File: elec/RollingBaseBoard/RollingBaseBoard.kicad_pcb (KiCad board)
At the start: 2 copper layers, 98 parts, among them P1 GP2, P10 UART_2, P11 I2C, P12 Motor, P13 Motor, P14 Encoder2, P15 Motor, P16 Switch, P17 Switch, P18 Switch, P19 Switch, P2 GP2, P20 Switch, P3 GP2, P4 GP2, P5 Bat5V, P6 Bat15V, P7 Encoder, P8 Encoder, P9 UART_1, U1 LMD18201, U2 LMD18201, U3 Teensy3.1

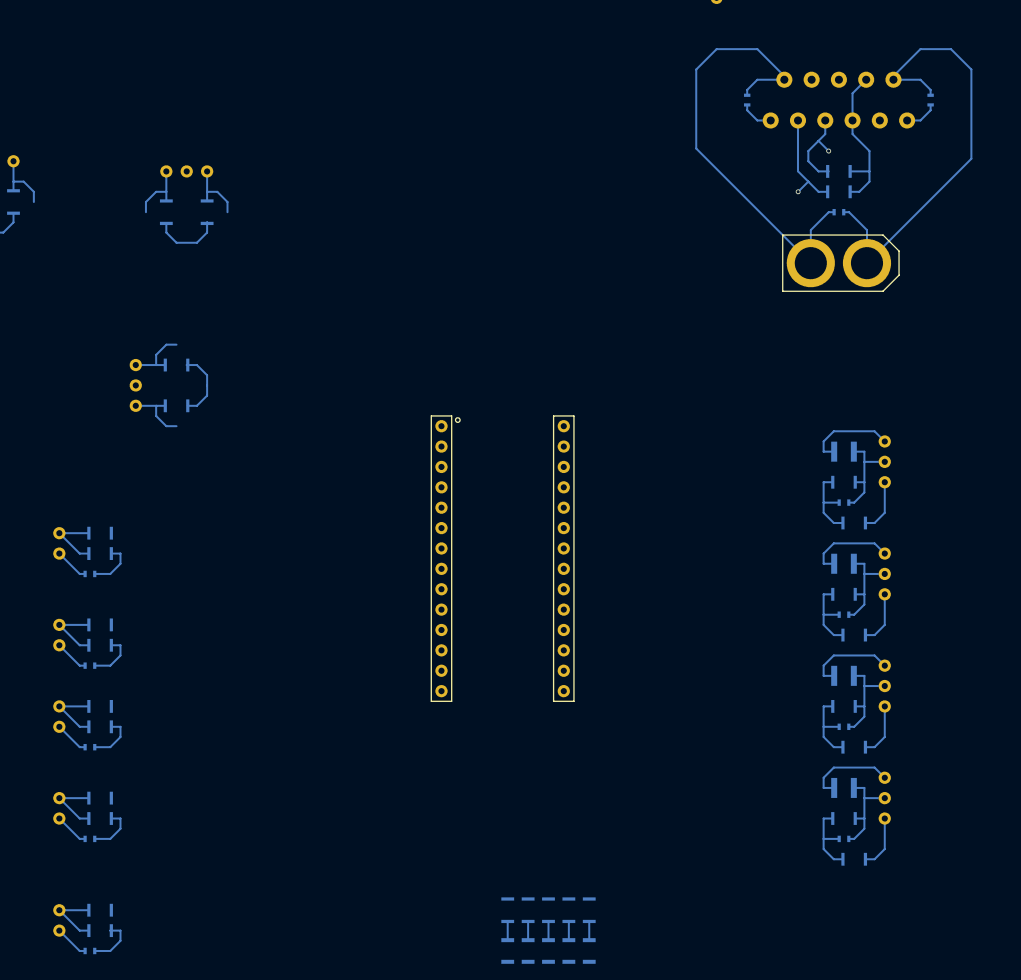
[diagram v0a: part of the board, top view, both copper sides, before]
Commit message: Progressing on rolling base board's routing
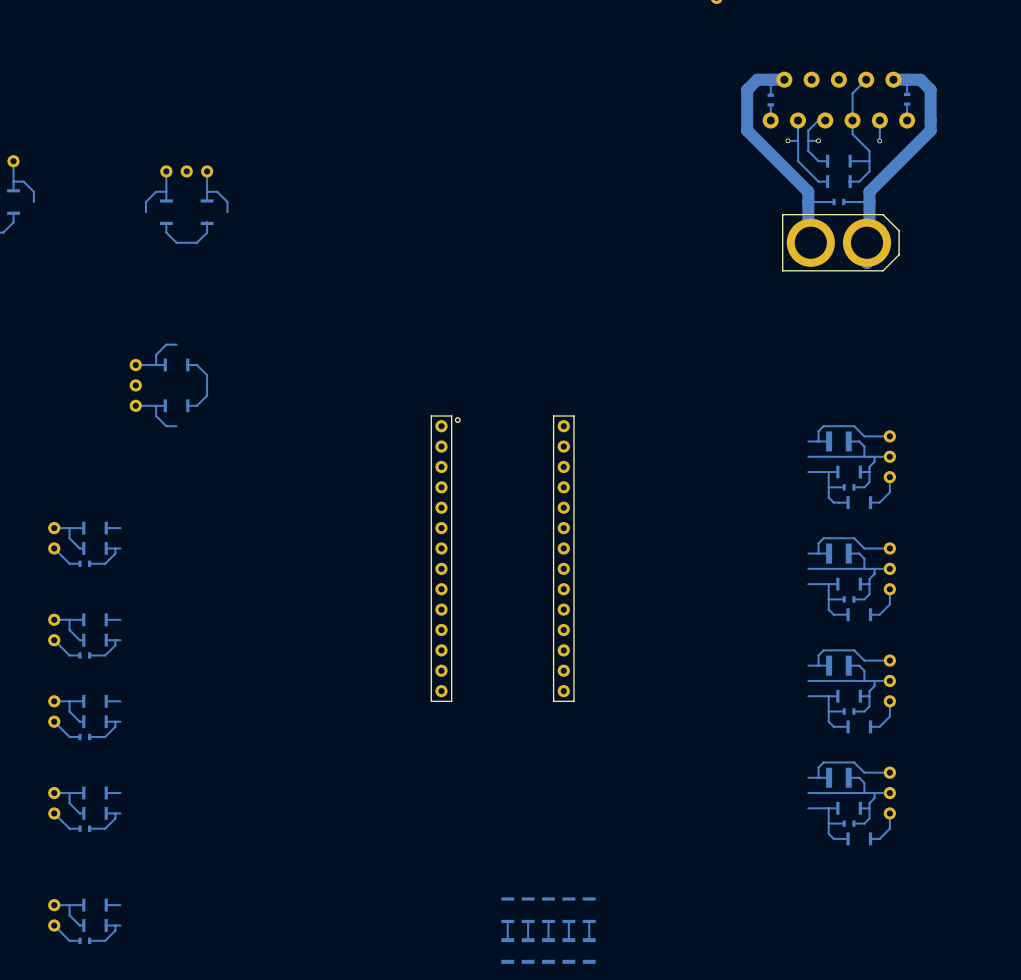
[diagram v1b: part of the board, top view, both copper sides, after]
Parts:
- moved C19 2.94 mm to (159.2, 38.1)
- moved C20 2.92 mm to (176.2, 38.0)
- moved R4 2.62 mm to (170.2, 116.2)
- moved R6 2.62 mm to (170.2, 102.2)
- moved R8 2.62 mm to (170.2, 88.3)
- moved R2 2.62 mm to (170.2, 130.2)
- moved P13 2.54 mm to (167.6, 55.9)
- moved C2 2.01 mm to (168.9, 128.3)
- moved C4 2.01 mm to (168.9, 114.3)
- moved C6 2.01 mm to (168.9, 100.3)
- moved C8 2.01 mm to (168.9, 86.4)
- moved C3 1.42 mm to (167.6, 108.6)
- moved C5 1.42 mm to (167.6, 94.6)
- moved C7 1.42 mm to (167.6, 80.6)
- moved C21 1.42 mm to (73.7, 142.9)
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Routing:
- net /Com/GND: track 142.9 -> 172.1 mm
- net Net-(C18-Pad2): track 57.7 -> 33.5 mm
- net Net-(C18-Pad1): track 55.9 -> 33.4 mm
- net /Com/+5V: track 84.8 -> 102.8 mm
- net /Driver_1/ThermalFlag: track 2.41 -> 4.96 mm, vias 0 -> 1
- net /Driver_2/PWM: track 11.7 -> 9.38 mm
- net Net-(C19-Pad1): track 4.13 -> 1.94 mm
- net Net-(C20-Pad2): track 4.13 -> 2.04 mm
- net Net-(P4-Pad1): track 6.75 -> 4.84 mm
- net Net-(P3-Pad1): track 6.75 -> 4.84 mm
- net Net-(P2-Pad1): track 6.75 -> 4.84 mm
- net Net-(P1-Pad1): track 6.75 -> 4.84 mm
- net /Driver_2/Direction: track 12.9 -> 11.1 mm
- net /Teensy/GP2_1: track 9.83 -> 11.5 mm
- net /Teensy/GP2_2: track 9.83 -> 11.5 mm
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
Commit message: Progressing on rolling base board's routing
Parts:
- added REF**: M4_Screw, Footprints:M4_Screw, F.Cu at (111.5, 142.0)
- added REF**: M4_Screw, Footprints:M4_Screw, F.Cu at (111.5, 68.0)
- added REF**: M4_Screw, Footprints:M4_Screw, F.Cu at (185.5, 68.0)
- added REF**: M4_Screw, Footprints:M4_Screw, F.Cu at (185.5, 142.0)
- D1, D2, D3, D4, D5, R28, R29, R30, R31, R32: moved to F.Cu
- moved P8 172.8 mm to (186.6, 78.3), turned to 270 degrees
- moved C10 166.7 mm to (182.8, 75.8), turned to 90 degrees
- moved R16 158.7 mm to (179.0, 79.6), turned to 180 degrees
- moved R17 158.7 mm to (179.0, 82.1), turned to 180 degrees
- moved R14 148.6 mm to (173.9, 79.6), turned to 0 degrees
- moved R15 148.5 mm to (173.9, 82.1), turned to 0 degrees
- moved P14 139.6 mm to (170.1, 80.9), turned to 90 degrees
- moved P16 117.3 mm to (146.0, 50.4), turned to 0 degrees
- moved C21 114.6 mm to (144.7, 52.9), turned to 90 degrees
- moved R34 113.9 mm to (147.2, 52.9), turned to 90 degrees
- moved R33 113.6 mm to (149.8, 52.9), turned to 90 degrees
- moved P5 104.8 mm to (148.5, 66.9)
- moved P18 102.9 mm to (161.2, 66.9), turned to 0 degrees
- moved C9 101.4 mm to (114.2, 80.9)
- moved R10 100.5 mm to (125.6, 77.1)
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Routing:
- net /Com/GND: track 172.1 -> 273.9 mm, vias 0 -> 13
- net /Com/+5V: track 102.8 -> 195.4 mm, vias 0 -> 7
- net Net-(P16-Pad2): track 7.25 -> 0.00 mm
- net /Teensy/Pull: track 6.28 -> 0.00 mm
- net /Teensy/LimitSwitch1: track 6.15 -> 9.96 mm
- net /Teensy/GP2_2: track 11.5 -> 14.7 mm
- net Net-(P3-Pad1): track 4.84 -> 2.41 mm
- net Net-(P2-Pad1): track 4.84 -> 2.41 mm
- net Net-(P4-Pad1): track 4.84 -> 6.75 mm
- net /Teensy/GP2_4: track 11.5 -> 9.98 mm
- net /Encoder_2/B: track 3.68 -> 2.41 mm
- net /Encoder_2/A: track 3.68 -> 2.41 mm
- net Net-(P8-Pad3): track 15.1 -> 16.3 mm
- net /Teensy/LimitSwitch2: track 6.15 -> 7.42 mm
- net Net-(P1-Pad1): track 4.84 -> 3.68 mm
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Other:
- board outline added: 80 x 80 mm

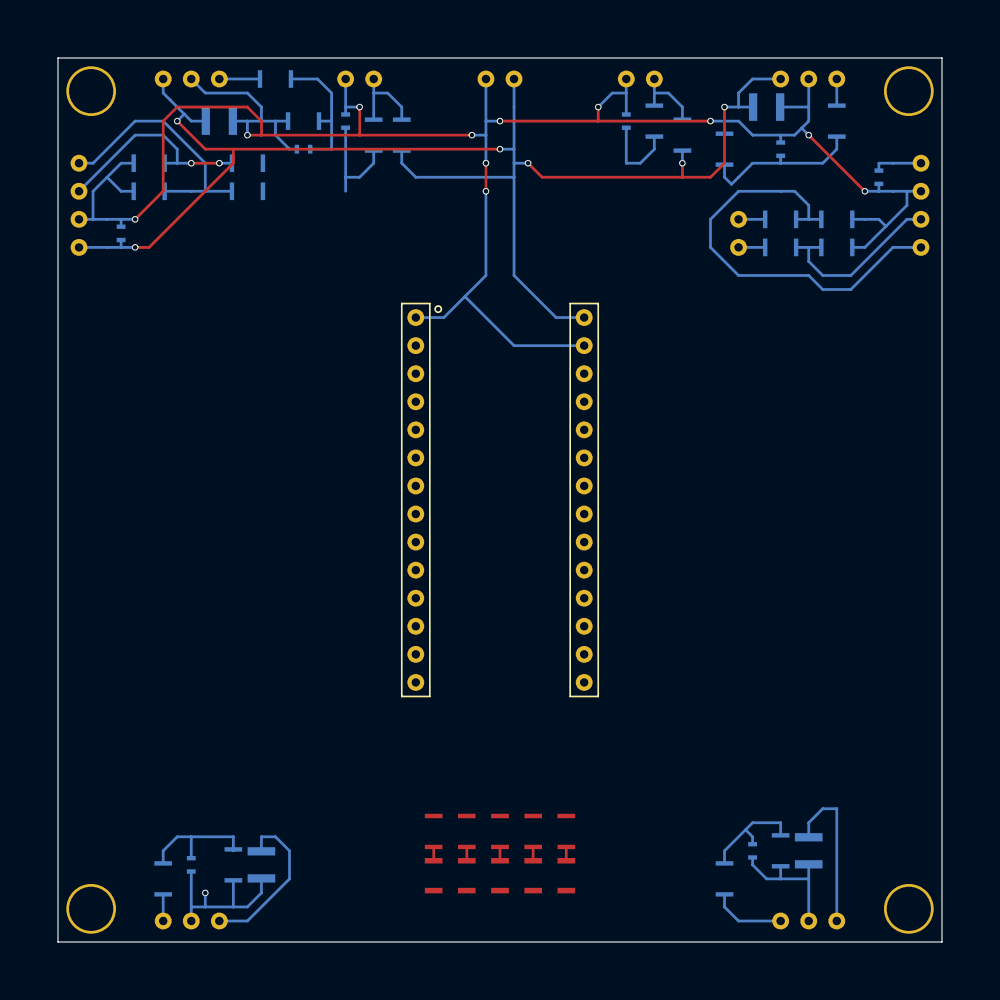
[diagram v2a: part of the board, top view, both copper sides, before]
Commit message: Replacing M4 screws with M3 ones
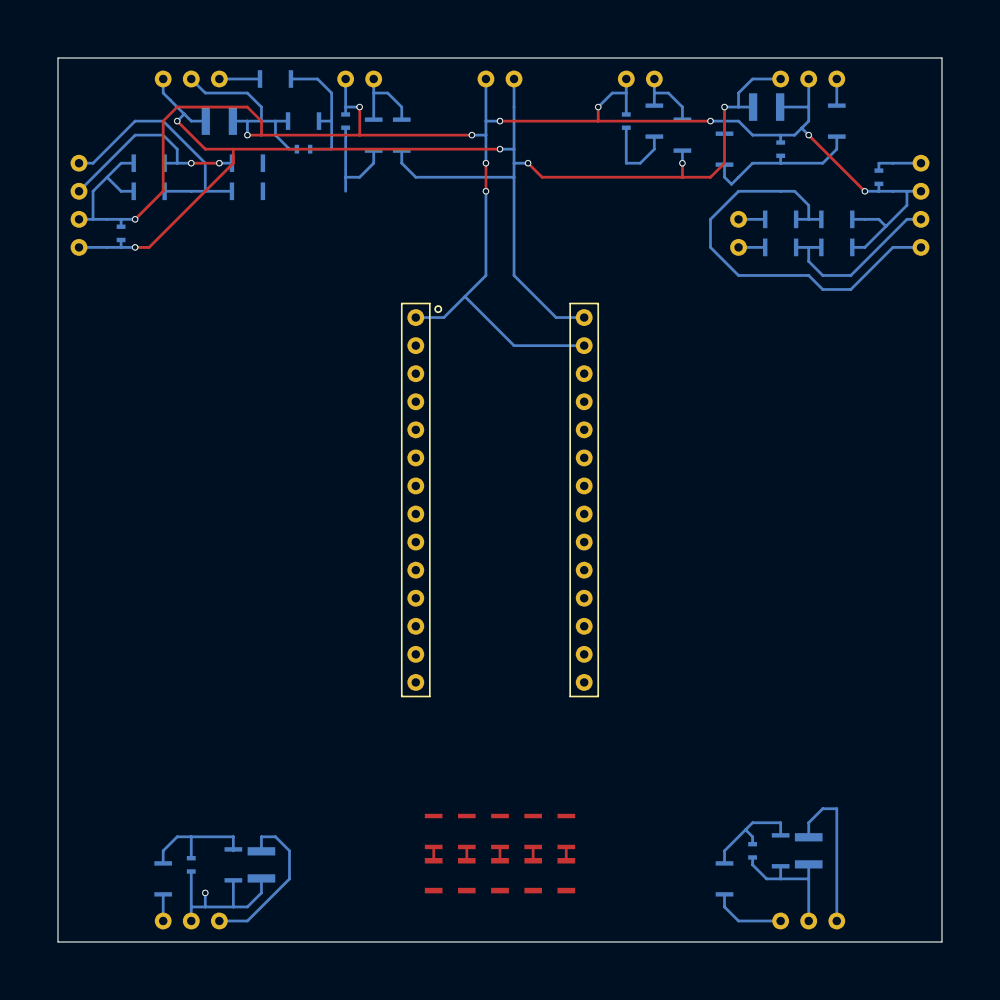
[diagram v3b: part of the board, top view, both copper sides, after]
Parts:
- removed REF** (x4): M4_Screw, Footprints:M4_Screw
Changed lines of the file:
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@@
-(kicad_pcb (version 4) (host pcbnew "(2015-09-24 BZR 6216, Git 45a9b1c)-product")
+(kicad_pcb (version 4) (host pcbnew 0.201509251831+6217~30~ubuntu15.04.1-product)
   (general
     (links 192)
     (no_connects 77)
-    (area 11.075 11.075 249.245002 148.277143)
+    (area 34.495 26.198 287.555002 163.625)
     (thickness 1.6)
     (drawings 4)
     (tracks 459)
     (zones 0)
-    (modules 102)
+    (modules 98)
     (nets 61)
   )
@@
       (net 57 "Net-(R30-Pad1)"))
   )
-  (module Footprints:M4_Screw (layer F.Cu)
-    (at 111.5 142)
-    (fp_text reference REF** (at 0 3.04) (layer F.SilkS) hide
-      (effects (font (size 1 1) (thickness 0.15)))
-    )
-    (fp_text value M4_Screw (at 0 -3.04) (layer F.Fab) hide
-      (effects (font (size 1 1) (thickness 0.15)))
-    )
-    (pad 1 thru_hole circle (at 0 0) (size 4.5 4.5) (drill 4) (layers *.Cu *.Mask F.SilkS))
-  )
-  (module Footprints:M4_Screw (layer F.Cu)
-    (at 111.5 68)
-    (fp_text reference REF** (at 0 3.04) (layer F.SilkS) hide
-      (effects (font (size 1 1) (thickness 0.15)))
-    )
-    (fp_text value M4_Screw (at 0 -3.04) (layer F.Fab) hide
-      (effects (font (size 1 1) (thickness 0.15)))
-    )
-    (pad 1 thru_hole circle (at 0 0) (size 4.5 4.5) (drill 4) (layers *.Cu *.Mask F.SilkS))
-  )
-  (module Footprints:M4_Screw (layer F.Cu)
-    (at 185.5 68)
-    (fp_text reference REF** (at 0 3.04) (layer F.SilkS) hide
-      (effects (font (size 1 1) (thickness 0.15)))
-    )
-    (fp_text value M4_Screw (at 0 -3.04) (layer F.Fab) hide
-      (effects (font (size 1 1) (thickness 0.15)))
-    )
-    (pad 1 thru_hole circle (at 0 0) (size 4.5 4.5) (drill 4) (layers *.Cu *.Mask F.SilkS))
-  )
-  (module Footprints:M4_Screw (layer F.Cu)
-    (at 185.5 142)
-    (fp_text reference REF** (at 0 3.04) (layer F.SilkS) hide
-      (effects (font (size 1 1) (thickness 0.15)))
-    )
-    (fp_text value M4_Screw (at 0 -3.04) (layer F.Fab) hide
-      (effects (font (size 1 1) (thickness 0.15)))
-    )
-    (pad 1 thru_hole circle (at 0 0) (size 4.5 4.5) (drill 4) (layers *.Cu *.Mask F.SilkS))
-  )
   (gr_line (start 108.5 145) (end 108.5 65) (angle 90) (layer Edge.Cuts) (width 0.1))

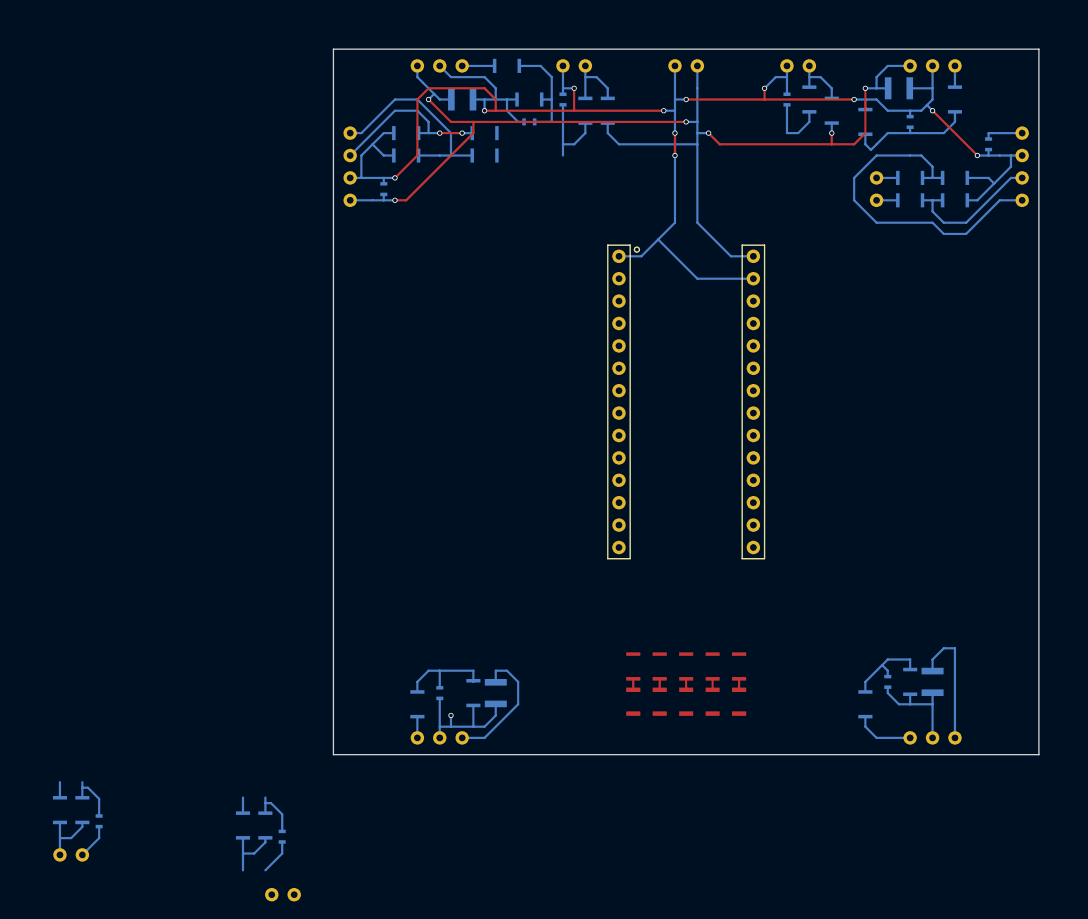
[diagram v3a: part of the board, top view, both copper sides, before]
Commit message: Progressing on the rolling base board
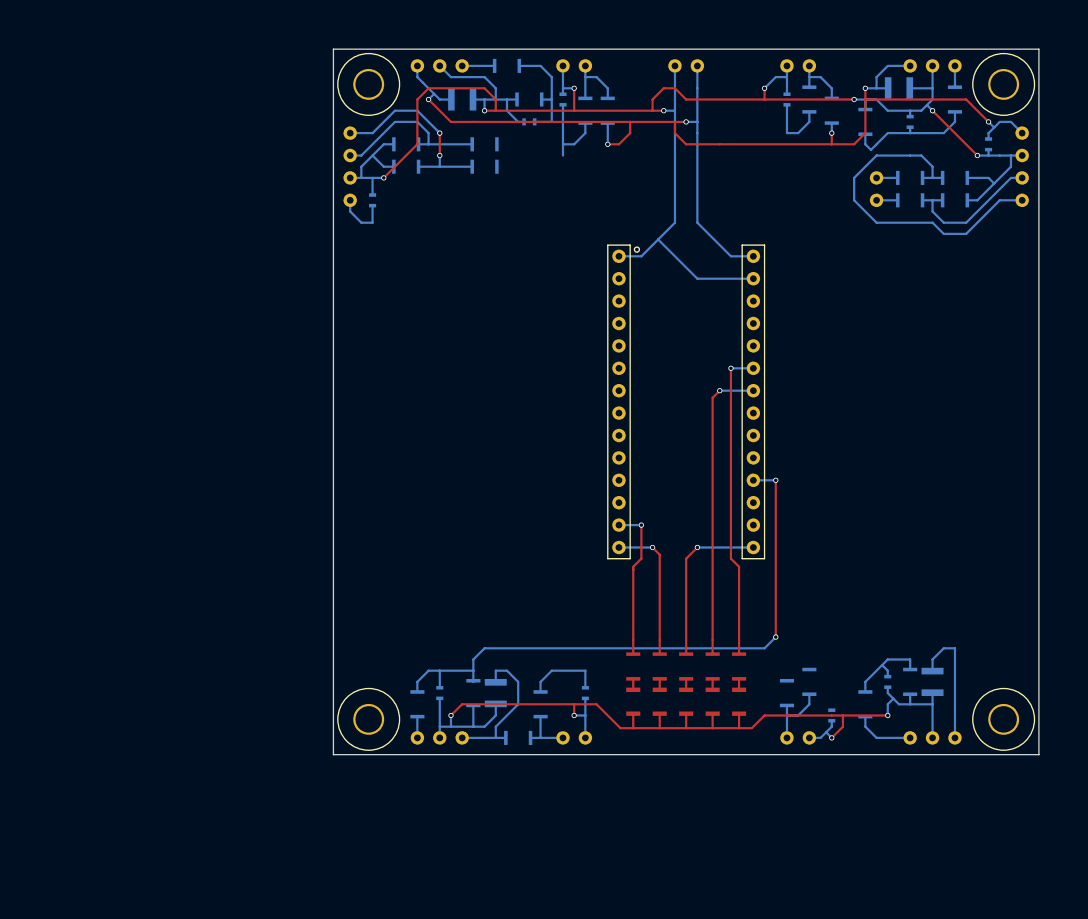
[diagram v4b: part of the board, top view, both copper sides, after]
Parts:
- added REF**: M3_Screw, Footprints:M3_Screw, F.Cu at (112.5, 69.0)
- added REF**: M3_Screw, Footprints:M3_Screw, F.Cu at (184.5, 69.0)
- added REF**: M3_Screw, Footprints:M3_Screw, F.Cu at (112.5, 141.0)
- added REF**: M3_Screw, Footprints:M3_Screw, F.Cu at (184.5, 141.0)
- moved C25 83.9 mm to (165.0, 140.6)
- moved R42 83.7 mm to (162.5, 136.8)
- moved R41 83.5 mm to (159.9, 138.0)
- moved P20 83.5 mm to (161.2, 143.1)
- moved C24 38.0 mm to (137.1, 138.0)
- moved P19 37.5 mm to (135.8, 143.1)
- moved R40 34.1 mm to (132.0, 139.3)
- moved R39 32.7 mm to (129.4, 143.1), turned to 0 degrees
- moved C9 1.80 mm to (112.9, 82.1)
- moved R11 1.27 mm to (125.6, 75.8)
- moved R13 1.27 mm to (116.8, 75.8)
- moved R10 1.27 mm to (125.6, 78.3)
- moved R12 1.27 mm to (116.8, 78.3)
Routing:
- net /Com/GND: track 273.9 -> 347.2 mm
- net /Teensy/GP2_3: track 11.4 -> 68.3 mm, vias 0 -> 2
- net Net-(R32-Pad1): track 0.00 -> 35.3 mm, vias 0 -> 1
- net Net-(R31-Pad1): track 0.00 -> 34.0 mm, vias 0 -> 1
- net Net-(R30-Pad1): track 0.00 -> 19.0 mm, vias 0 -> 1
- net Net-(R28-Pad1): track 0.00 -> 17.6 mm, vias 0 -> 1
- net Net-(R29-Pad1): track 0.00 -> 16.2 mm, vias 0 -> 1
- net /Teensy/LimitSwitch4: track 6.15 -> 0.00 mm
- net /Teensy/LimitSwitch3: track 6.15 -> 8.69 mm
- net /Com/+5V: track 195.4 -> 196.7 mm
- net Net-(P19-Pad2): track 7.25 -> 6.09 mm
- net Net-(P7-Pad4): track 23.2 -> 22.2 mm, vias 0 -> 2
- net Net-(P20-Pad2): track 7.25 -> 7.89 mm
- net Net-(P7-Pad3): track 18.9 -> 18.4 mm, vias 2 -> 0

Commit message: Progressing on the rolling base board
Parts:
- moved P15 162.1 mm to (88.8, 92.3), turned to 90 degrees
- moved R1 155.6 mm to (95.2, 92.3)
- moved C15 127.4 mm to (172.6, 112.6), turned to 0 degrees
- moved R26 124.7 mm to (102.8, 105.0), turned to 270 degrees
- moved C11 124.3 mm to (177.7, 126.6)
- moved C12 124.1 mm to (180.2, 125.3)
- moved CP1 123.8 mm to (182.8, 122.8)
- moved R27 123.3 mm to (105.3, 105.0), turned to 90 degrees
- moved C17 123.3 mm to (112.9, 120.2)
- moved CP2 121.8 mm to (123.1, 124.0), turned to 180 degrees
- moved C16 118.2 mm to (118.0, 121.5)
- moved C13 115.5 mm to (163.7, 105.0), turned to 90 degrees
- moved C20 113.8 mm to (124.4, 97.4), turned to 180 degrees
- moved U2 112.0 mm to (120.6, 105.0), turned to 90 degrees
- moved P6 110.1 mm to (112.9, 130.4), turned to 270 degrees
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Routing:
- net /Com/GND: track 347.2 -> 514.0 mm
- net /Driver_1/+15V: track 0.00 -> 124.2 mm
- net /Teensy/GP2_1: track 12.4 -> 71.3 mm, vias 0 -> 2
- net /Teensy/GP2_2: track 14.7 -> 61.7 mm
- net /Teensy/LimitSwitch4: track 0.00 -> 47.0 mm, vias 0 -> 2
- net /Driver_2/PWM: track 9.38 -> 53.9 mm, vias 1 -> 2
- net /Com/+5V: track 196.7 -> 240.3 mm, vias 7 -> 11
- net /Teensy/LimitSwitch2: track 7.42 -> 47.8 mm, vias 0 -> 2
- net /Driver_1/PWM: track 10.7 -> 50.5 mm, vias 1 -> 2
- net /Teensy/GP2_4: track 9.98 -> 44.7 mm, vias 0 -> 2
- net /Encoder_1/B: track 0.00 -> 31.5 mm
- net /Encoder_1/A: track 0.00 -> 30.7 mm
- net /Teensy/LimitSwitch1: track 9.96 -> 40.0 mm, vias 0 -> 2
- net /Teensy/LimitSwitch3: track 8.69 -> 38.4 mm, vias 0 -> 2
- net Net-(C13-Pad2): track 57.7 -> 31.4 mm
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
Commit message: Completing rolling base board, only a few minor fixes are left to do
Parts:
- moved P11 99.2 mm to (171.4, 121.5)
- moved R22 87.9 mm to (166.3, 119.0), turned to 0 degrees
- moved R23 87.9 mm to (166.3, 124.0), turned to 0 degrees
- moved P15 78.9 mm to (167.6, 87.2), turned to 0 degrees
- moved R1 72.4 mm to (167.6, 91.0)
- moved P16 71.1 mm to (125.6, 83.4)
- moved R34 69.0 mm to (129.4, 83.4)
- moved R33 69.0 mm to (132.0, 83.4)
- moved C21 68.8 mm to (126.9, 86.0), turned to 180 degrees
- moved R26 63.2 mm to (161.2, 80.9), turned to 0 degrees
- moved P10 47.6 mm to (135.8, 110.1)
- moved R20 43.7 mm to (134.5, 101.2)
- moved R21 43.4 mm to (137.1, 103.7), turned to 270 degrees
- moved R27 41.4 mm to (144.7, 92.3), turned to 270 degrees
- moved R18 35.0 mm to (119.3, 82.1), turned to 0 degrees
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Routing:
- net /Com/GND: track 514.0 -> 666.2 mm, vias 13 -> 24
- net /Com/+5V: track 240.3 -> 355.5 mm, vias 11 -> 16
- net /Driver_1/ThermalFlag: track 0.00 -> 105.8 mm, vias 0 -> 6
- net /Driver_2/Direction: track 0.00 -> 87.2 mm, vias 0 -> 5
- net /Com/TX1: track 0.00 -> 47.0 mm, vias 0 -> 2
- net /Com/RX1: track 0.00 -> 36.8 mm
- net /Com/SDA: track 0.00 -> 27.2 mm, vias 0 -> 2
- net /Com/SCL: track 0.00 -> 22.4 mm, vias 0 -> 2
- net /Teensy/Pull: track 0.00 -> 21.7 mm, vias 0 -> 2
- net /Driver_1/Direction: track 0.00 -> 21.0 mm, vias 0 -> 2
- net /Com/TX2: track 0.00 -> 20.5 mm, vias 0 -> 2
- net /Com/RX2: track 0.00 -> 15.6 mm, vias 0 -> 2
- net /Driver_2/PWM: track 53.9 -> 69.3 mm
- net Net-(P16-Pad2): track 0.00 -> 11.1 mm
- net /Teensy/GP2_1: track 71.3 -> 79.5 mm
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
